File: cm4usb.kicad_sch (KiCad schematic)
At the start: 24 parts, among them J6 USB4110-GF-A, J7 USB4110-GF-A, U14 USB3740B-AI2, U15 AP22653FDZ-7

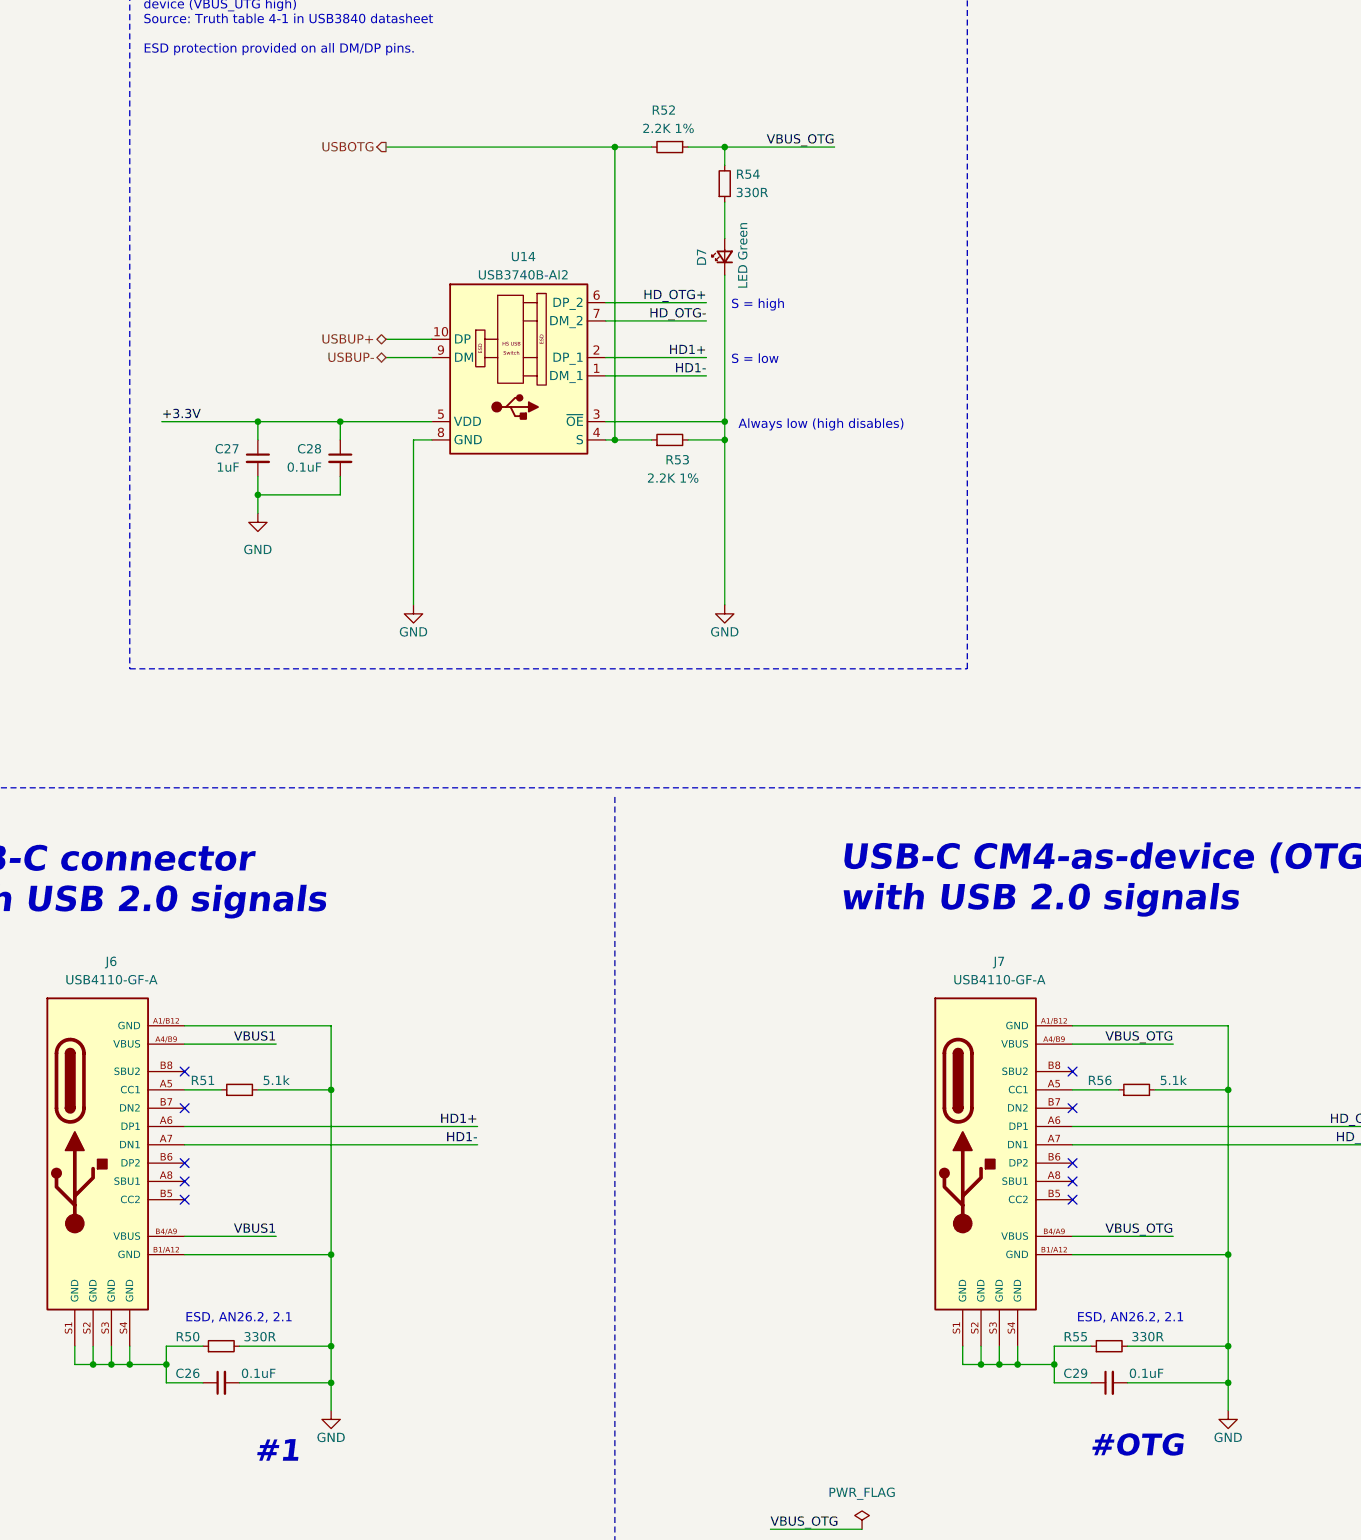
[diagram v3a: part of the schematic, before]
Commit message: merging changes for face plate conn
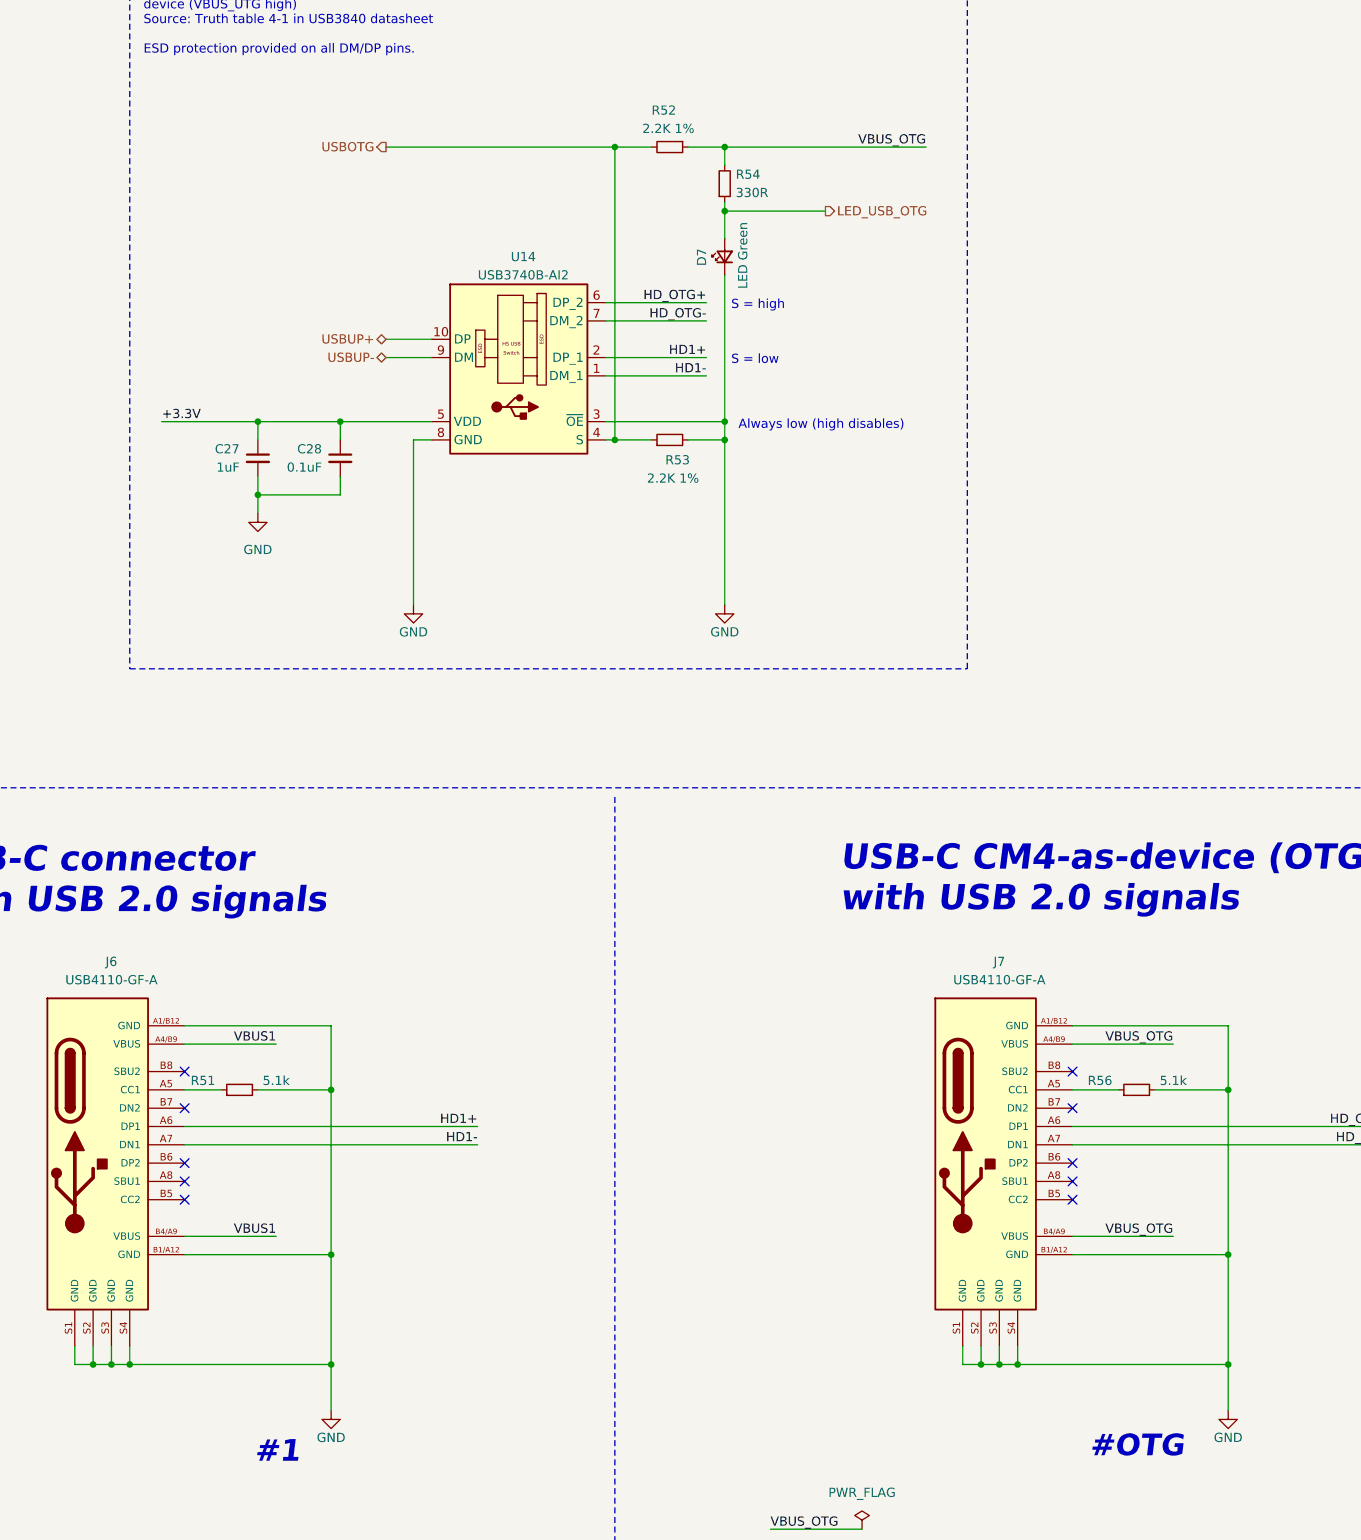
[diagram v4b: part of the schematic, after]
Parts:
- removed C26, C29: 0.1uF, Capacitor_SMD:C_0402_1005Metric, symbol Device:C_Small
- removed R50, R55: 330R, Resistor_SMD:R_0402_1005Metric, symbol Device:R_Small
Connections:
- net GND: now also J6.S1 (GND), J6.S2 (GND), J6.S3 (GND), J6.S4 (GND), J7.S1 (GND), J7.S2 (GND), J7.S3 (GND), J7.S4 (GND)
- net LED_USB_OTG: now reaches D7.2 (A), R54.1
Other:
- note removed: "ESD, AN26.2, 2.1"

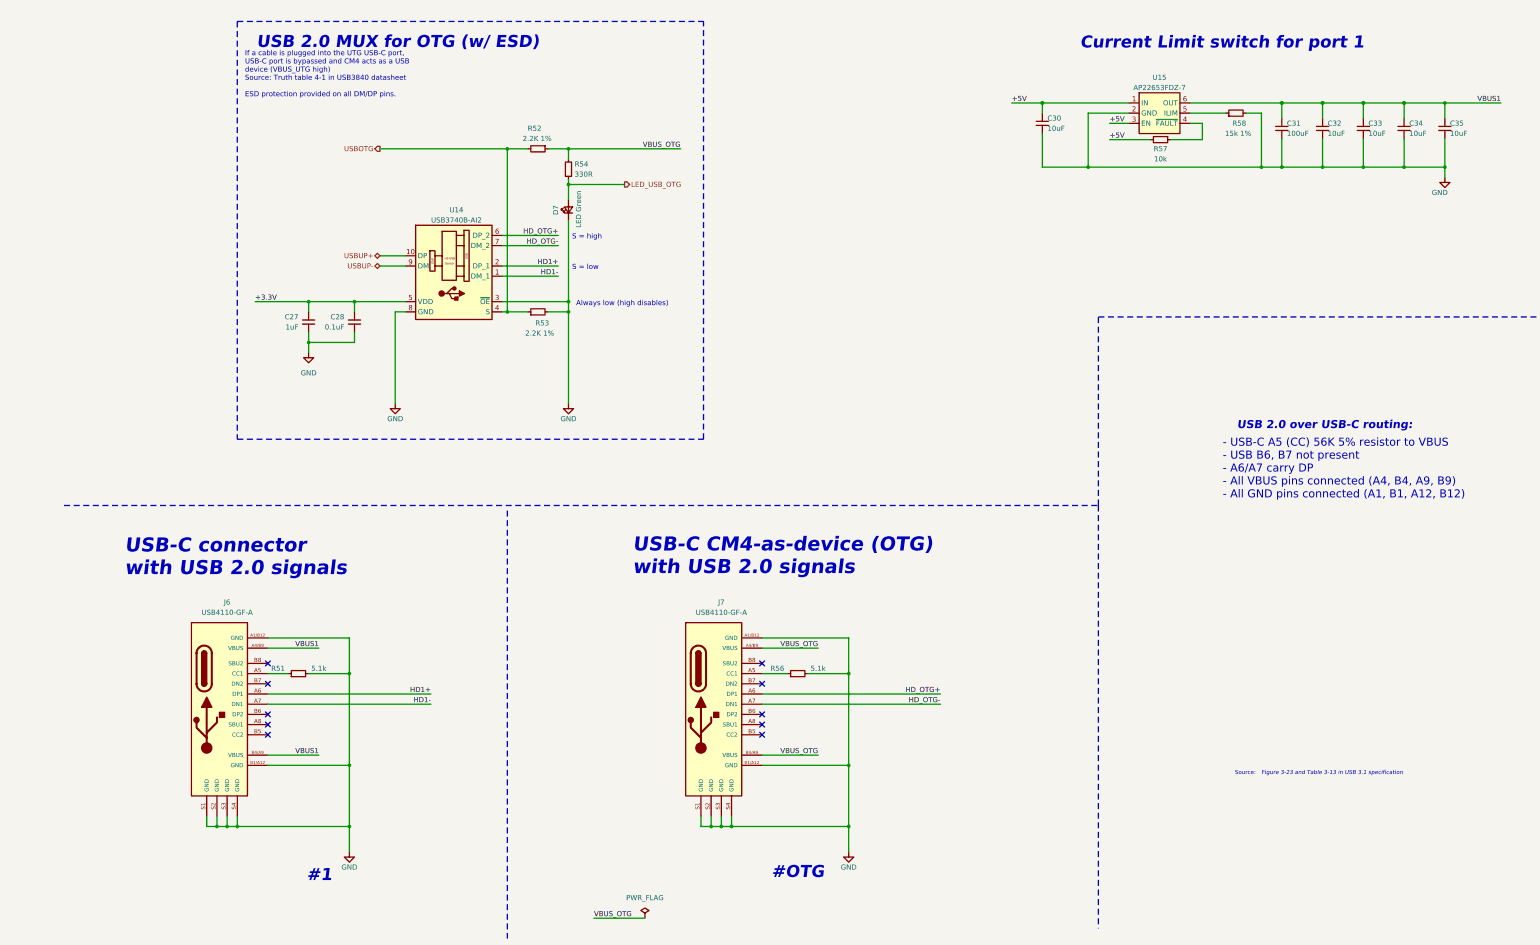
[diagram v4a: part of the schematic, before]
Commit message: connecterized faceplate, refreshed schematic
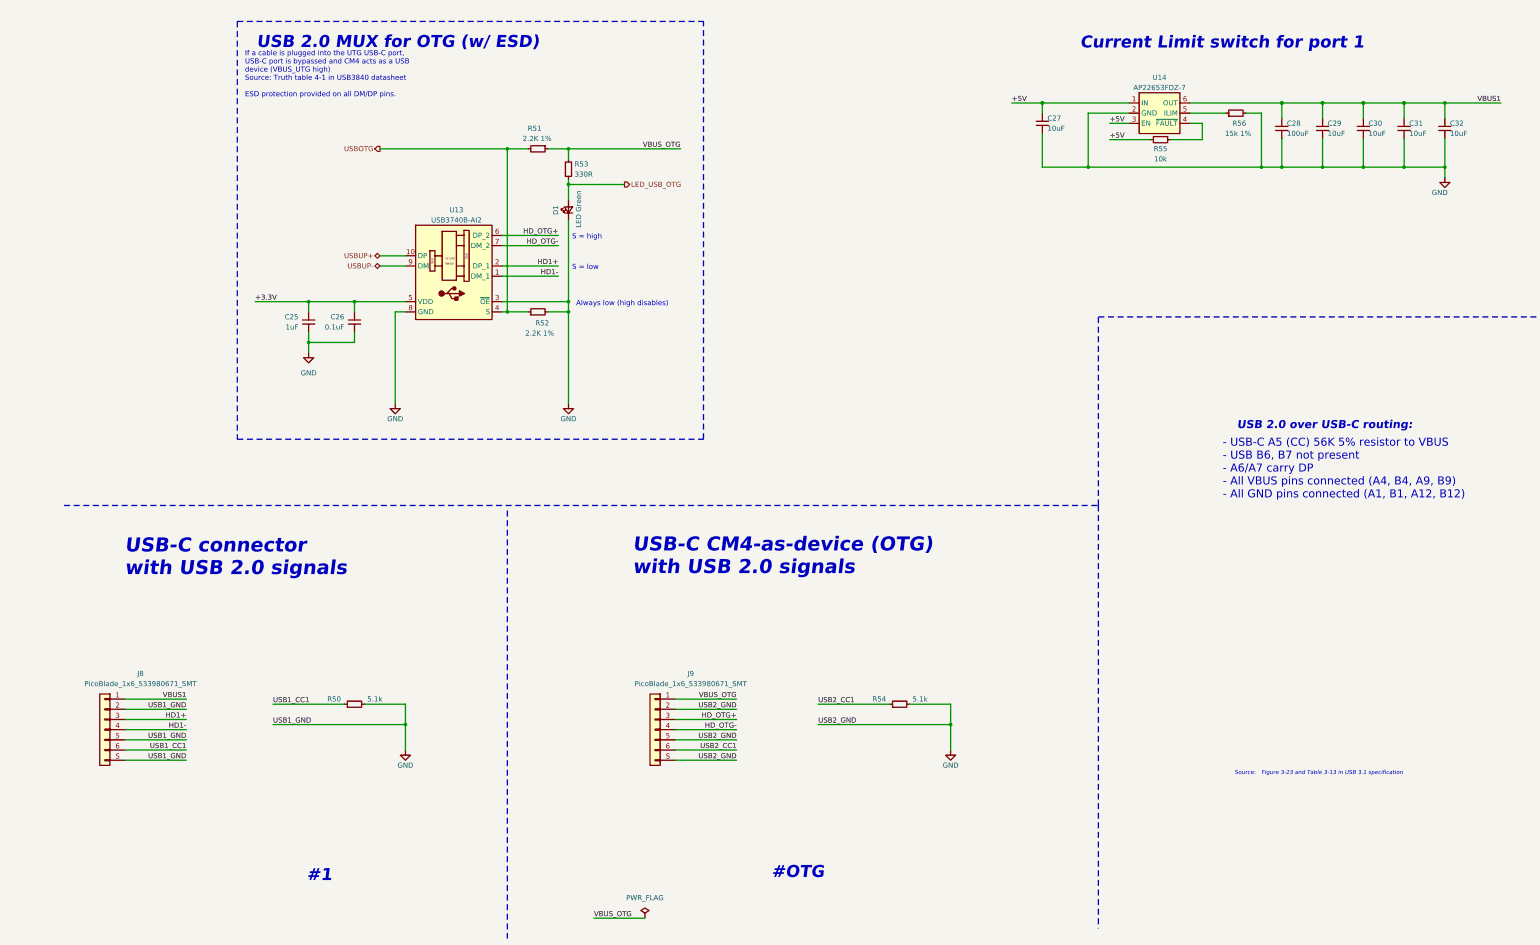
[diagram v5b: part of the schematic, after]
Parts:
- removed J6, J7: USB4110-GF-A, Connector_USB_GCT:USB4110-GF-A, symbol Connector_USB_GCT:USB4110-GF-A
- added J8, J9: PicoBlade_1x6_533980671_SMT, Connector_PicoBlade_Molex:MOLEX_533980671, symbol Connector_PicoBlade_Molex:PicoBlade_1x6_533980671_SMT
- renumbered C27 to C25, C28 to C26, C30 to C27, C31 to C28, C32 to C29, C33 to C30, C34 to C31, C35 to C32, D7 to D1, R51 to R50, R52 to R51, R53 to R52, R54 to R53, R56 to R54, R57 to R55, R58 to R56, U14 to U13, U15 to U14
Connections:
- net GND: now also J8.2 (Pin_2), J8.5 (Pin_5), J8.S (SHIELD), J9.2 (Pin_2), J9.5 (Pin_5), J9.S (SHIELD)
- net HD1+: now also J8.3 (Pin_3)
- net HD1-: now also J8.4 (Pin_4)
- net HD_OTG+: now also J9.3 (Pin_3)
- net HD_OTG-: now also J9.4 (Pin_4)
- net VBUS1: now also J8.1 (Pin_1)
- net VBUS_OTG: now also J9.1 (Pin_1)
- net USB2_CC1: now reaches R54.1
- net USB2_CC1: now also J9.6 (Pin_6)
- net USB1_CC1: now reaches R50.1
- net USB1_CC1: now also J8.6 (Pin_6)
- no-connect marks 10 -> 0
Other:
- moved on the sheet: R50, R54

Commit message: led changes
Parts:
- removed D1: LED Green, LED_SMD_LiteOn:LED_0603_1608Metric_green, symbol Device:LED_Small
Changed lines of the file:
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@@
   (junction (at 347.98 76.2) (diameter 1.016) (color 0 0 0 0)
   )
-  (junction (at 149.86 96.52) (diameter 0) (color 0 0 0 0)
-  )
   (junction (at 358.14 92.202) (diameter 0.9144) (color 0 0 0 0)
   )
@@
   )
   (junction (at 368.3 92.202) (diameter 0.9144) (color 0 0 0 0)
-  )
-  (junction (at 149.86 125.73) (diameter 0.9144) (color 0 0 0 0)
   )
   (junction (at 327.66 92.202) (diameter 0.9144) (color 0 0 0 0)
@@
     (stroke (width 0) (type solid) (color 0 0 0 0))
   )
-  (wire (pts (xy 149.86 96.52) (xy 149.86 100.33))
-    (stroke (width 0) (type solid) (color 0 0 0 0))
-  )
   (wire (pts (xy 176.53 232.41) (xy 191.77 232.41))
     (stroke (width 0) (type default) (color 0 0 0 0))
@@
   (wire (pts (xy 39.37 227.33) (xy 54.61 227.33))
     (stroke (width 0) (type default) (color 0 0 0 0))
-  )
-  (wire (pts (xy 149.86 105.41) (xy 149.86 125.73))
-    (stroke (width 0) (type solid) (color 0 0 0 0))
   )
   (wire (pts (xy 284.734 85.344) (xy 294.894 85.344))
@@
       (effects (font (size 1.27 1.27)) hide)
     )
-    (pin "1")
-    (pin "2")
-  )
-  (symbol (lib_id "Device:LED_Small") (at 149.86 102.87 90) (unit 1)
-    (in_bom yes) (on_board yes)
-    (property "Reference" "D1" (id 0) (at 146.685 104.14 0)
-      (effects (font (size 1.27 1.27)) (justify left))
-    )
-    (property "Value" "LED Green" (id 1) (at 152.4 107.315 0)
-      (effects (font (size 1.27 1.27)) (justify left))
-    )
-    (property "Footprint" "LED_SMD_LiteOn:LED_0603_1608Metric_green" (id 2) (at 149.86 102.87 90)
-      (effects (font (size 1.27 1.27)) hide)
-    )
-    (property "Datasheet" "~" (id 3) (at 149.86 102.87 90)
-      (effects (font (size 1.27 1.27)) hide)
-    )
